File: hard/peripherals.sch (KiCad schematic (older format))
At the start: 12 parts, among them J2 PJ-3062-CO, U1 ADXL362BCCZ-RLX, U2 ADXL345BCCZ-RL7

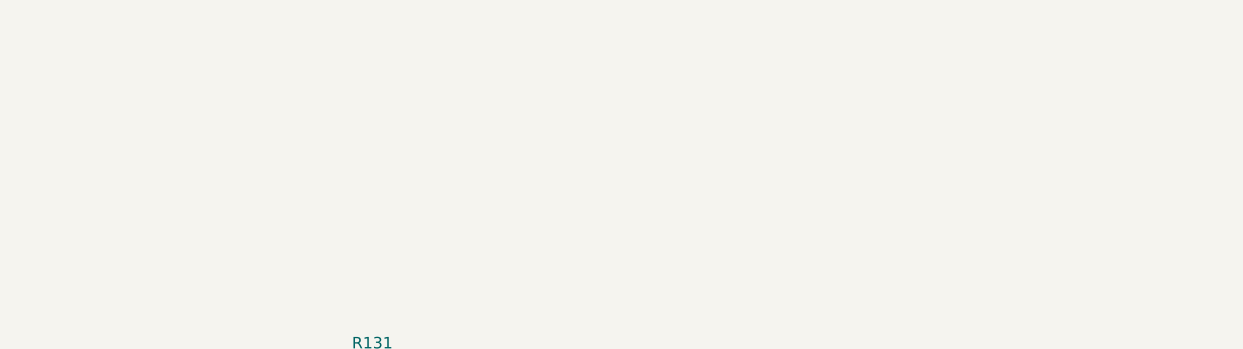
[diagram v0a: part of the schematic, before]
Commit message: led matrix schematic page completed
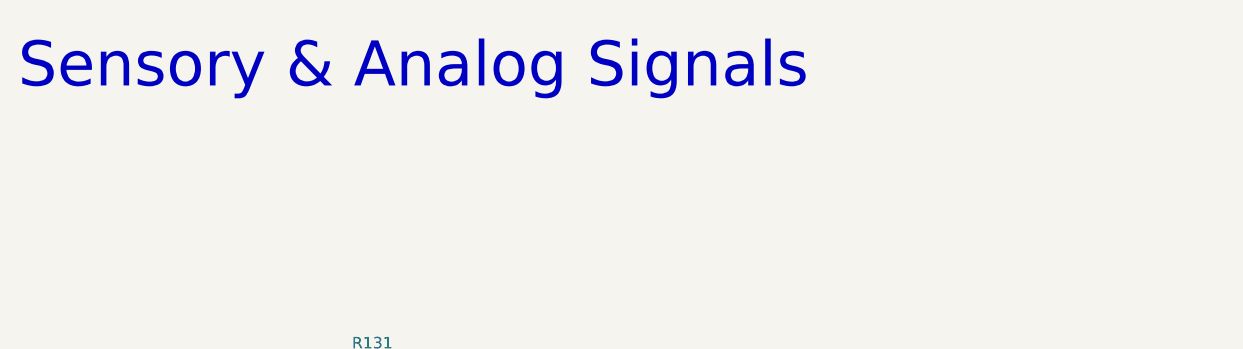
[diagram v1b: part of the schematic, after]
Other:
- note added: "Sensory & Analog Signals"
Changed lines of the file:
@@
 $Descr A4 11693 8268
 encoding utf-8
-Sheet 5 5
+Sheet 69 69
 Title ""
 Date ""
@@
 Wire Wire Line
 	4250 4050 4250 3950
+Text Notes 1900 1800 0    197  ~ 0
+Sensory & Analog Signals
 $EndSCHEMATC

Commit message: pc format refactor wip
@lukekaese leds still need to be attenuated
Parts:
- renumbered R131 to R196, R132 to R197
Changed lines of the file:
@@
 $EndComp
 $Comp
-L power:+3V3 #PWR0104
+L power:+3V3 #PWR0182
 U 1 1 613EF1A2
 P 7650 1800
-F 0 "#PWR0104" H 7650 1650 50  0001 C CNN
+F 0 "#PWR0182" H 7650 1650 50  0001 C CNN
 F 1 "+3V3" H 7665 1973 50  0000 C CNN
 F 2 "" H 7650 1800 50  0001 C CNN
@@
 $EndComp
 $Comp
-L power:GND #PWR0105
+L power:GND #PWR0183
 U 1 1 613F21F8
 P 7650 2600
-F 0 "#PWR0105" H 7650 2350 50  0001 C CNN
+F 0 "#PWR0183" H 7650 2350 50  0001 C CNN
 F 1 "GND" H 7655 2427 50  0000 C CNN
 F 2 "" H 7650 2600 50  0001 C CNN
@@
 $EndComp
 $Comp
-L power:+3V3 #PWR0102
+L power:+3V3 #PWR0180
 U 1 1 61439963
 P 7550 4450
-F 0 "#PWR0102" H 7550 4300 50  0001 C CNN
+F 0 "#PWR0180" H 7550 4300 50  0001 C CNN
 F 1 "+3V3" H 7565 4623 50  0000 C CNN
 F 2 "" H 7550 4450 50  0001 C CNN
@@
 	8200 4600 8200 4650
 $Comp
-L power:GND #PWR0103
+L power:GND #PWR0181
 U 1 1 6143C822
 P 7550 5150
-F 0 "#PWR0103" H 7550 4900 50  0001 C CNN
+F 0 "#PWR0181" H 7550 4900 50  0001 C CNN
 F 1 "GND" H 7555 4977 50  0000 C CNN
 F 2 "" H 7550 5150 50  0001 C CNN
@@
 $EndComp
 $Comp
-L power:GND #PWR096
+L power:GND #PWR0174
 U 1 1 6147785D
 P 2600 3200
-F 0 "#PWR096" H 2600 2950 50  0001 C CNN
+F 0 "#PWR0174" H 2600 2950 50  0001 C CNN
 F 1 "GND" V 2605 3072 50  0000 R CNN
 F 2 "" H 2600 3200 50  0001 C CNN
@@
 $EndComp
 $Comp
-L power:GND #PWR097
+L power:GND #PWR0175
 U 1 1 614784D6
 P 2600 3400
-F 0 "#PWR097" H 2600 3150 50  0001 C CNN
+F 0 "#PWR0175" H 2600 3150 50  0001 C CNN
 F 1 "GND" V 2605 3272 50  0000 R CNN
 F 2 "" H 2600 3400 50  0001 C CNN
@@
 $EndComp
 $Comp
-L power:GND #PWR098
+L power:GND #PWR0176
 U 1 1 614787FA
 P 2600 3600
-F 0 "#PWR098" H 2600 3350 50  0001 C CNN
+F 0 "#PWR0176" H 2600 3350 50  0001 C CNN
 F 1 "GND" V 2605 3472 50  0000 R CNN
 F 2 "" H 2600 3600 50  0001 C CNN
@@
 analog_tip
 $Comp
-L Device:R R131
+L Device:R R196
 U 1 1 6147E21F
 P 3450 3100
-F 0 "R131" V 3243 3100 50  0000 C CNN
+F 0 "R196" V 3243 3100 50  0000 C CNN
 F 1 "100R" V 3334 3100 50  0000 C CNN
 F 2 "Resistor_SMD:R_0603_1608Metric" V 3380 3100 50  0001 C CNN
@@
 $EndComp
 $Comp
-L Device:R R132
+L Device:R R197
 U 1 1 6147FCF6
 P 3450 3500
-F 0 "R132" V 3657 3500 50  0000 C CNN
+F 0 "R197" V 3657 3500 50  0000 C CNN
 F 1 "100R" V 3566 3500 50  0000 C CNN
 F 2 "Resistor_SMD:R_0603_1608Metric" V 3380 3500 50  0001 C CNN
@@
 Connection ~ 4250 3100
 $Comp
-L power:GND #PWR099
+L power:GND #PWR0177
 U 1 1 614B8C36
 P 3100 4050
-F 0 "#PWR099" H 3100 3800 50  0001 C CNN
+F 0 "#PWR0177" H 3100 3800 50  0001 C CNN
 F 1 "GND" H 3105 3877 50  0000 C CNN
 F 2 "" H 3100 4050 50  0001 C CNN
@@
 $EndComp
 $Comp
-L power:GND #PWR0100
+L power:GND #PWR0178
 U 1 1 614B947F
 P 3750 4050
-F 0 "#PWR0100" H 3750 3800 50  0001 C CNN
+F 0 "#PWR0178" H 3750 3800 50  0001 C CNN
 F 1 "GND" H 3755 3877 50  0000 C CNN
 F 2 "" H 3750 4050 50  0001 C CNN
@@
 $EndComp
 $Comp
-L power:GND #PWR0101
+L power:GND #PWR0179
 U 1 1 614B9A2A
 P 4250 4050
-F 0 "#PWR0101" H 4250 3800 50  0001 C CNN
+F 0 "#PWR0179" H 4250 3800 50  0001 C CNN
 F 1 "GND" H 4255 3877 50  0000 C CNN
 F 2 "" H 4250 4050 50  0001 C CNN

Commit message: layouting update
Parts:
- renumbered C9 to C22, C11 to C23, C8 to C24, C10 to C25, D1035 to D1025, D1036 to D1026, D1034 to D1027
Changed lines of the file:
@@
 $EndDescr
 $Comp
-L Device:C C11
+L Device:C C23
 U 1 1 613EB9FD
 P 8300 2150
-F 0 "C11" H 8186 2104 50  0000 R CNN
+F 0 "C23" H 8186 2104 50  0000 R CNN
 F 1 "0u1/6V3" H 8186 2195 50  0000 R CNN
 F 2 "Capacitor_SMD:C_0402_1005Metric" H 8338 2000 50  0001 C CNN
@@
 $EndComp
 $Comp
-L Device:C C9
+L Device:C C22
 U 1 1 613EE98F
 P 7700 2150
-F 0 "C9" H 7586 2104 50  0000 R CNN
+F 0 "C22" H 7586 2104 50  0000 R CNN
 F 1 "0u1/6V3" H 7586 2195 50  0000 R CNN
 F 2 "Capacitor_SMD:C_0402_1005Metric" H 7738 2000 50  0001 C CNN
@@
 $EndComp
 $Comp
-L power:+3V3 #PWR0182
+L power:+3V3 #PWR0191
 U 1 1 613EF1A2
 P 7650 1800
-F 0 "#PWR0182" H 7650 1650 50  0001 C CNN
+F 0 "#PWR0191" H 7650 1650 50  0001 C CNN
 F 1 "+3V3" H 7665 1973 50  0000 C CNN
 F 2 "" H 7650 1800 50  0001 C CNN
@@
 $EndComp
 $Comp
-L power:GND #PWR0183
+L power:GND #PWR0192
 U 1 1 613F21F8
 P 7650 2600
-F 0 "#PWR0183" H 7650 2350 50  0001 C CNN
+F 0 "#PWR0192" H 7650 2350 50  0001 C CNN
 F 1 "GND" H 7655 2427 50  0000 C CNN
 F 2 "" H 7650 2600 50  0001 C CNN
@@
 $EndComp
 $Comp
-L Device:C C10
+L Device:C C25
 U 1 1 614359EF
 P 8200 4800
-F 0 "C10" H 8086 4754 50  0000 R CNN
+F 0 "C25" H 8086 4754 50  0000 R CNN
 F 1 "0u1/6V3" H 8086 4845 50  0000 R CNN
 F 2 "Capacitor_SMD:C_0402_1005Metric" H 8238 4650 50  0001 C CNN
@@
 $EndComp
 $Comp
-L Device:C C8
+L Device:C C24
 U 1 1 614361F4
 P 7600 4800
-F 0 "C8" H 7486 4754 50  0000 R CNN
+F 0 "C24" H 7486 4754 50  0000 R CNN
 F 1 "1u/6V3" H 7486 4845 50  0000 R CNN
 F 2 "Capacitor_SMD:C_0603_1608Metric" H 7638 4650 50  0001 C CNN
@@
 $EndComp
 $Comp
-L power:+3V3 #PWR0180
+L power:+3V3 #PWR0199
 U 1 1 61439963
 P 7550 4450
-F 0 "#PWR0180" H 7550 4300 50  0001 C CNN
+F 0 "#PWR0199" H 7550 4300 50  0001 C CNN
 F 1 "+3V3" H 7565 4623 50  0000 C CNN
 F 2 "" H 7550 4450 50  0001 C CNN
@@
 	8200 4600 8200 4650
 $Comp
-L power:GND #PWR0181
+L power:GND #PWR0200
 U 1 1 6143C822
 P 7550 5150
-F 0 "#PWR0181" H 7550 4900 50  0001 C CNN
+F 0 "#PWR0200" H 7550 4900 50  0001 C CNN
 F 1 "GND" H 7555 4977 50  0000 C CNN
 F 2 "" H 7550 5150 50  0001 C CNN
@@
 $EndComp
 $Comp
-L power:GND #PWR0174
+L power:GND #PWR0193
 U 1 1 6147785D
 P 2600 3200
-F 0 "#PWR0174" H 2600 2950 50  0001 C CNN
+F 0 "#PWR0193" H 2600 2950 50  0001 C CNN
 F 1 "GND" V 2605 3072 50  0000 R CNN
 F 2 "" H 2600 3200 50  0001 C CNN
@@
 $EndComp
 $Comp
-L power:GND #PWR0175
+L power:GND #PWR0194
 U 1 1 614784D6
 P 2600 3400
-F 0 "#PWR0175" H 2600 3150 50  0001 C CNN
+F 0 "#PWR0194" H 2600 3150 50  0001 C CNN
 F 1 "GND" V 2605 3272 50  0000 R CNN
 F 2 "" H 2600 3400 50  0001 C CNN
@@
 $EndComp
 $Comp
-L power:GND #PWR0176
+L power:GND #PWR0195
 U 1 1 614787FA
 P 2600 3600
-F 0 "#PWR0176" H 2600 3350 50  0001 C CNN
+F 0 "#PWR0195" H 2600 3350 50  0001 C CNN
 F 1 "GND" V 2605 3472 50  0000 R CNN
 F 2 "" H 2600 3600 50  0001 C CNN
@@
 $EndComp
 $Comp
-L led_matrix:PSM712-LF-T7 D1034
+L led_matrix:PSM712-LF-T7 D1027
 U 1 1 61497024
 P 3250 3850
-F 0 "D1034" V 3250 3878 50  0000 L CNN
+F 0 "D1027" V 3250 3878 50  0000 L CNN
 F 1 "PSM712-LF-T7" H 3250 3900 50  0001 C CNN
 F 2 "Package_TO_SOT_SMD:SOT-23" H 3250 3850 50  0001 C CNN
@@
 $EndComp
 $Comp
-L Device:D_Zener D1035
+L Device:D_Zener D1025
 U 1 1 614A4095
 P 3750 3800
-F 0 "D1035" V 3704 3880 50  0000 L CNN
+F 0 "D1025" V 3704 3880 50  0000 L CNN
 F 1 "D_Zener" V 3795 3880 50  0000 L CNN
 F 2 "Diode_SMD:D_MiniMELF" H 3750 3800 50  0001 C CNN
@@
 $EndComp
 $Comp
-L Device:D_Zener D1036
+L Device:D_Zener D1026
 U 1 1 614AA758
 P 4250 3800
-F 0 "D1036" V 4204 3880 50  0000 L CNN
+F 0 "D1026" V 4204 3880 50  0000 L CNN
 F 1 "D_Zener" V 4295 3880 50  0000 L CNN
 F 2 "Diode_SMD:D_MiniMELF" H 4250 3800 50  0001 C CNN
@@
 Connection ~ 4250 3100
 $Comp
-L power:GND #PWR0177
+L power:GND #PWR0196
 U 1 1 614B8C36
 P 3100 4050
-F 0 "#PWR0177" H 3100 3800 50  0001 C CNN
+F 0 "#PWR0196" H 3100 3800 50  0001 C CNN
 F 1 "GND" H 3105 3877 50  0000 C CNN
 F 2 "" H 3100 4050 50  0001 C CNN
@@
 $EndComp
 $Comp
-L power:GND #PWR0178
+L power:GND #PWR0197
 U 1 1 614B947F
 P 3750 4050
-F 0 "#PWR0178" H 3750 3800 50  0001 C CNN
+F 0 "#PWR0197" H 3750 3800 50  0001 C CNN
 F 1 "GND" H 3755 3877 50  0000 C CNN
 F 2 "" H 3750 4050 50  0001 C CNN
@@
 $EndComp
 $Comp
-L power:GND #PWR0179
+L power:GND #PWR0198
 U 1 1 614B9A2A
 P 4250 4050
-F 0 "#PWR0179" H 4250 3800 50  0001 C CNN
+F 0 "#PWR0198" H 4250 3800 50  0001 C CNN
 F 1 "GND" H 4255 3877 50  0000 C CNN
 F 2 "" H 4250 4050 50  0001 C CNN

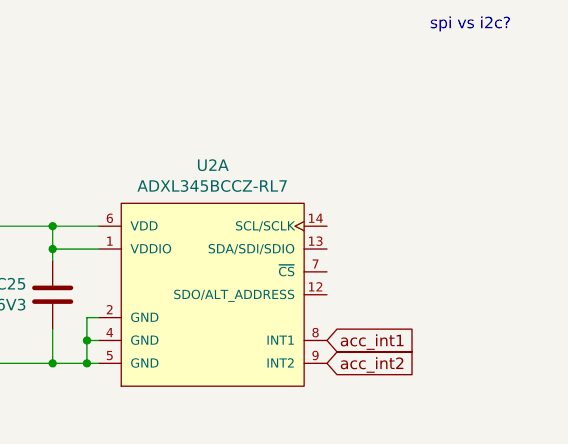
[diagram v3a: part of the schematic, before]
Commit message: connected uc to matrix line driver signals
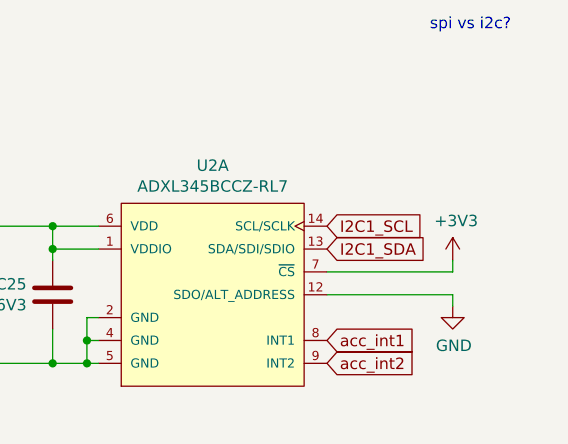
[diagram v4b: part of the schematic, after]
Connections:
- net +3V3: now also U2.7 (~CS~)
- net GND: now also U2.12 (SDO/ALT_ADDRESS)
- net I2C1_SDA: now reaches U2.13 (SDA/SDI/SDIO)
- net I2C1_SCL: now reaches U2.14 (SCL/SCLK)
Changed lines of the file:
@@
 Text Notes 1900 1800 0    197  ~ 0
 Sensory & Analog Signals
+Text GLabel 9400 4500 2    50   Input ~ 0
+I2C1_SCL
+Text GLabel 9400 4600 2    50   Input ~ 0
+I2C1_SDA
+$Comp
+L power:+3V3 #PWR0210
+U 1 1 627632FA
+P 9950 4650
+F 0 "#PWR0210" H 9950 4500 50  0001 C CNN
+F 1 "+3V3" H 9965 4823 50  0000 C CNN
+F 2 "" H 9950 4650 50  0001 C CNN
+F 3 "" H 9950 4650 50  0001 C CNN
+	1    9950 4650
+	1    0    0    -1
+$EndComp
+$Comp
+L power:GND #PWR0211
+U 1 1 62764EA2
+P 9950 4850
+F 0 "#PWR0211" H 9950 4600 50  0001 C CNN
+F 1 "GND" H 9955 4677 50  0000 C CNN
+F 2 "" H 9950 4850 50  0001 C CNN
+F 3 "" H 9950 4850 50  0001 C CNN
+	1    9950 4850
+	1    0    0    -1
+$EndComp
+Wire Wire Line
+	9400 4700 9950 4700
+Wire Wire Line
+	9950 4700 9950 4650
+Wire Wire Line
+	9400 4800 9950 4800
+Wire Wire Line
+	9950 4800 9950 4850
 $EndSCHEMATC

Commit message: pcb format refactor
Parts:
- renumbered C22 to C24, C23 to C25, C24 to C26, C25 to C27, D1025 to D1026, D1026 to D1027, D1027 to D1028, J2 to J3, R196 to R206, R197 to R207
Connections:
- net at J3.R, R206.2: now also D1028.2; no longer D1028.1
- net at J3.T, R207.1: now also D1028.1; no longer D1028.2
- net analog_ring renamed 3MM5_RING
- net analog_tip renamed 3MM5_TIP
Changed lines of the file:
@@
 $EndDescr
 $Comp
-L Device:C C23
+L Device:C C25
 U 1 1 613EB9FD
 P 8300 2150
-F 0 "C23" H 8186 2104 50  0000 R CNN
+F 0 "C25" H 8186 2104 50  0000 R CNN
 F 1 "0u1/6V3" H 8186 2195 50  0000 R CNN
 F 2 "Capacitor_SMD:C_0402_1005Metric" H 8338 2000 50  0001 C CNN
@@
 $EndComp
 $Comp
-L Device:C C22
+L Device:C C24
 U 1 1 613EE98F
 P 7700 2150
-F 0 "C22" H 7586 2104 50  0000 R CNN
+F 0 "C24" H 7586 2104 50  0000 R CNN
 F 1 "0u1/6V3" H 7586 2195 50  0000 R CNN
 F 2 "Capacitor_SMD:C_0402_1005Metric" H 7738 2000 50  0001 C CNN
@@
 $EndComp
 $Comp
-L power:+3V3 #PWR0191
+L power:+3V3 #PWR0200
 U 1 1 613EF1A2
 P 7650 1800
-F 0 "#PWR0191" H 7650 1650 50  0001 C CNN
+F 0 "#PWR0200" H 7650 1650 50  0001 C CNN
 F 1 "+3V3" H 7665 1973 50  0000 C CNN
 F 2 "" H 7650 1800 50  0001 C CNN
@@
 $EndComp
 $Comp
-L power:GND #PWR0192
+L power:GND #PWR0201
 U 1 1 613F21F8
 P 7650 2600
-F 0 "#PWR0192" H 7650 2350 50  0001 C CNN
+F 0 "#PWR0201" H 7650 2350 50  0001 C CNN
 F 1 "GND" H 7655 2427 50  0000 C CNN
 F 2 "" H 7650 2600 50  0001 C CNN
@@
 $EndComp
 $Comp
-L Device:C C25
+L Device:C C27
 U 1 1 614359EF
 P 8200 4800
-F 0 "C25" H 8086 4754 50  0000 R CNN
+F 0 "C27" H 8086 4754 50  0000 R CNN
 F 1 "0u1/6V3" H 8086 4845 50  0000 R CNN
 F 2 "Capacitor_SMD:C_0402_1005Metric" H 8238 4650 50  0001 C CNN
@@
 $EndComp
 $Comp
-L Device:C C24
+L Device:C C26
 U 1 1 614361F4
 P 7600 4800
-F 0 "C24" H 7486 4754 50  0000 R CNN
+F 0 "C26" H 7486 4754 50  0000 R CNN
 F 1 "1u/6V3" H 7486 4845 50  0000 R CNN
 F 2 "Capacitor_SMD:C_0603_1608Metric" H 7638 4650 50  0001 C CNN
@@
 $EndComp
 $Comp
-L power:+3V3 #PWR0199
+L power:+3V3 #PWR0208
 U 1 1 61439963
 P 7550 4450
-F 0 "#PWR0199" H 7550 4300 50  0001 C CNN
+F 0 "#PWR0208" H 7550 4300 50  0001 C CNN
 F 1 "+3V3" H 7565 4623 50  0000 C CNN
 F 2 "" H 7550 4450 50  0001 C CNN
@@
 	8200 4600 8200 4650
 $Comp
-L power:GND #PWR0200
+L power:GND #PWR0211
 U 1 1 6143C822
 P 7550 5150
-F 0 "#PWR0200" H 7550 4900 50  0001 C CNN
+F 0 "#PWR0211" H 7550 4900 50  0001 C CNN
 F 1 "GND" H 7555 4977 50  0000 C CNN
 F 2 "" H 7550 5150 50  0001 C CNN
@@
 spi vs i2c?
 $Comp
-L Connector:AudioJack3_SwitchTR J2
+L Connector:AudioJack3_SwitchTR J3
 U 1 1 6146E8AE
 P 2400 3300
-F 0 "J2" H 2382 3625 50  0000 C CNN
+F 0 "J3" H 2382 3625 50  0000 C CNN
 F 1 "PJ-3062-CO" H 2382 3534 50  0000 C CNN
 F 2 "led_matrix:Connectors_XKB Connectivity_PJ-3062-CO" H 2400 3300 50  0001 C CNN
@@
 $EndComp
 $Comp
-L power:GND #PWR0193
+L power:GND #PWR0202
 U 1 1 6147785D
 P 2600 3200
-F 0 "#PWR0193" H 2600 2950 50  0001 C CNN
+F 0 "#PWR0202" H 2600 2950 50  0001 C CNN
 F 1 "GND" V 2605 3072 50  0000 R CNN
 F 2 "" H 2600 3200 50  0001 C CNN
@@
 $EndComp
 $Comp
-L power:GND #PWR0194
+L power:GND #PWR0203
 U 1 1 614784D6
 P 2600 3400
-F 0 "#PWR0194" H 2600 3150 50  0001 C CNN
+F 0 "#PWR0203" H 2600 3150 50  0001 C CNN
 F 1 "GND" V 2605 3272 50  0000 R CNN
 F 2 "" H 2600 3400 50  0001 C CNN
@@
 $EndComp
 $Comp
-L power:GND #PWR0195
+L power:GND #PWR0204
 U 1 1 614787FA
 P 2600 3600
-F 0 "#PWR0195" H 2600 3350 50  0001 C CNN
+F 0 "#PWR0204" H 2600 3350 50  0001 C CNN
 F 1 "GND" V 2605 3472 50  0000 R CNN
 F 2 "" H 2600 3600 50  0001 C CNN
@@
 $EndComp
 Text GLabel 4500 3100 2    50   Input ~ 0
-analog_ring
+3MM5_RING
 Text GLabel 4500 3500 2    50   Input ~ 0
-analog_tip
-$Comp
-L Device:R R196
+3MM5_TIP
+$Comp
+L Device:R R206
 U 1 1 6147E21F
 P 3450 3100
-F 0 "R196" V 3243 3100 50  0000 C CNN
+F 0 "R206" V 3243 3100 50  0000 C CNN
 F 1 "100R" V 3334 3100 50  0000 C CNN
 F 2 "Resistor_SMD:R_0603_1608Metric" V 3380 3100 50  0001 C CNN
@@
 $EndComp
 $Comp
-L Device:R R197
+L Device:R R207
 U 1 1 6147FCF6
 P 3450 3500
-F 0 "R197" V 3657 3500 50  0000 C CNN
+F 0 "R207" V 3657 3500 50  0000 C CNN
 F 1 "100R" V 3566 3500 50  0000 C CNN
 F 2 "Resistor_SMD:R_0603_1608Metric" V 3380 3500 50  0001 C CNN
@@
 $EndComp
 $Comp
-L led_matrix:PSM712-LF-T7 D1027
+L led_matrix:PSM712-LF-T7 D1028
 U 1 1 61497024
 P 3250 3850
-F 0 "D1027" V 3250 3878 50  0000 L CNN
+F 0 "D1028" V 3250 3878 50  0000 L CNN
 F 1 "PSM712-LF-T7" H 3250 3900 50  0001 C CNN
 F 2 "Package_TO_SOT_SMD:SOT-23" H 3250 3850 50  0001 C CNN
@@
 $EndComp
 $Comp
-L Device:D_Zener D1025
+L Device:D_Zener D1026
 U 1 1 614A4095
 P 3750 3800
-F 0 "D1025" V 3704 3880 50  0000 L CNN
+F 0 "D1026" V 3704 3880 50  0000 L CNN
 F 1 "D_Zener" V 3795 3880 50  0000 L CNN
 F 2 "Diode_SMD:D_MiniMELF" H 3750 3800 50  0001 C CNN
@@
 $EndComp
 $Comp
-L Device:D_Zener D1026
+L Device:D_Zener D1027
 U 1 1 614AA758
 P 4250 3800
-F 0 "D1026" V 4204 3880 50  0000 L CNN
+F 0 "D1027" V 4204 3880 50  0000 L CNN
 F 1 "D_Zener" V 4295 3880 50  0000 L CNN
 F 2 "Diode_SMD:D_MiniMELF" H 4250 3800 50  0001 C CNN
@@
 $EndComp
 Wire Wire Line
-	2600 3500 3000 3500
-Wire Wire Line
-	3000 3600 3000 3500
-Connection ~ 3000 3500
-Wire Wire Line
-	3000 3500 3300 3500
-Wire Wire Line
-	3200 3600 3200 3300
-Wire Wire Line
-	3200 3300 2600 3300
-Wire Wire Line
-	3200 3300 3200 3100
-Wire Wire Line
-	3200 3100 3300 3100
-Connection ~ 3200 3300
-Wire Wire Line
 	3600 3100 4250 3100
 Wire Wire Line
@@
 Connection ~ 4250 3100
 $Comp
-L power:GND #PWR0196
+L power:GND #PWR0205
 U 1 1 614B8C36
 P 3100 4050
-F 0 "#PWR0196" H 3100 3800 50  0001 C CNN
+F 0 "#PWR0205" H 3100 3800 50  0001 C CNN
 F 1 "GND" H 3105 3877 50  0000 C CNN
 F 2 "" H 3100 4050 50  0001 C CNN
@@
 $EndComp
 $Comp
-L power:GND #PWR0197
+L power:GND #PWR0206
 U 1 1 614B947F
 P 3750 4050
-F 0 "#PWR0197" H 3750 3800 50  0001 C CNN
+F 0 "#PWR0206" H 3750 3800 50  0001 C CNN
 F 1 "GND" H 3755 3877 50  0000 C CNN
 F 2 "" H 3750 4050 50  0001 C CNN
@@
 $EndComp
 $Comp
-L power:GND #PWR0198
+L power:GND #PWR0207
 U 1 1 614B9A2A
 P 4250 4050
-F 0 "#PWR0198" H 4250 3800 50  0001 C CNN
+F 0 "#PWR0207" H 4250 3800 50  0001 C CNN
 F 1 "GND" H 4255 3877 50  0000 C CNN
 F 2 "" H 4250 4050 50  0001 C CNN
@@
 I2C1_SDA
 $Comp
-L power:+3V3 #PWR0210
+L power:+3V3 #PWR0209
 U 1 1 627632FA
 P 9950 4650
-F 0 "#PWR0210" H 9950 4500 50  0001 C CNN
+F 0 "#PWR0209" H 9950 4500 50  0001 C CNN
 F 1 "+3V3" H 9965 4823 50  0000 C CNN
 F 2 "" H 9950 4650 50  0001 C CNN
@@
 $EndComp
 $Comp
-L power:GND #PWR0211
+L power:GND #PWR0210
 U 1 1 62764EA2
 P 9950 4850
-F 0 "#PWR0211" H 9950 4600 50  0001 C CNN
+F 0 "#PWR0210" H 9950 4600 50  0001 C CNN
 F 1 "GND" H 9955 4677 50  0000 C CNN
 F 2 "" H 9950 4850 50  0001 C CNN
@@
 Wire Wire Line
 	9950 4800 9950 4850
+Wire Wire Line
+	2600 3500 3200 3500
+Wire Wire Line
+	3000 3600 3000 3300
+Connection ~ 3000 3300
+Wire Wire Line
+	3000 3300 2600 3300
+Wire Wire Line
+	3000 3300 3000 3100
+Wire Wire Line
+	3000 3100 3300 3100
+Wire Wire Line
+	3200 3600 3200 3500
+Connection ~ 3200 3500
+Wire Wire Line
+	3200 3500 3300 3500
 $EndSCHEMATC
